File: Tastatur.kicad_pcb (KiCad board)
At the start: 2 copper layers, 74.8 x 41.4 mm, 86 parts, among them Q1 SI2301CDS-T1-GE3, Q2 2N7002HW, U1 CH592F, U3 AZ1117-3.3, U4 MT3608, U5 74LVC1G08, U6 LM393, U7 USBLC6-2SC6

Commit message: update power mgmt
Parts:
- removed D33, D4: LED, LED_SMD:LED_0603_1608Metric_Pad1.05x0.95mm_HandSolder
- removed D38, D39: CUS10S30,H3F, Diode_SMD:D_SOD-323
- removed R14, R15, R16, R17, R18, R19, R20, R21, R22, R23, R24, R25, R26, R27: 1 kohm, Resistor_SMD:R_0603_1608Metric_Pad0.98x0.95mm_HandSolder
- removed U2: ~, steew:ADNS-5090
- added C10: 100N, Capacitor_SMD:C_0603_1608Metric_Pad1.08x0.95mm_HandSolder, F.Cu at (168.6, 56.8)
- added C11: 100N, Capacitor_SMD:C_0603_1608Metric_Pad1.08x0.95mm_HandSolder, F.Cu at (168.6, 59.3)
- added C12: 100N, Capacitor_SMD:C_0603_1608Metric_Pad1.08x0.95mm_HandSolder, F.Cu at (168.6, 61.8)
- added C13: 100N, Capacitor_SMD:C_0603_1608Metric_Pad1.08x0.95mm_HandSolder, F.Cu at (168.6, 64.3)
- added C14: 100N, Capacitor_SMD:C_0603_1608Metric_Pad1.08x0.95mm_HandSolder, F.Cu at (172.9, 49.3)
- added C15: 100N, Capacitor_SMD:C_0603_1608Metric_Pad1.08x0.95mm_HandSolder, F.Cu at (172.9, 51.8)
- added C16: 100N, Capacitor_SMD:C_0603_1608Metric_Pad1.08x0.95mm_HandSolder, F.Cu at (172.9, 54.3)
- added C17: 100N, Capacitor_SMD:C_0603_1608Metric_Pad1.08x0.95mm_HandSolder, F.Cu at (172.9, 56.8)
- added C18: 100N, Capacitor_SMD:C_0603_1608Metric_Pad1.08x0.95mm_HandSolder, F.Cu at (172.9, 59.3)
- added C19: 100N, Capacitor_SMD:C_0603_1608Metric_Pad1.08x0.95mm_HandSolder, F.Cu at (172.9, 61.8)
- added C20: 100N, Capacitor_SMD:C_0603_1608Metric_Pad1.08x0.95mm_HandSolder, F.Cu at (172.9, 64.3)
- added C21: 100N, Capacitor_SMD:C_0603_1608Metric_Pad1.08x0.95mm_HandSolder, F.Cu at (177.3, 49.3)
- added C22: 100N, Capacitor_SMD:C_0603_1608Metric_Pad1.08x0.95mm_HandSolder, F.Cu at (147.4, 68.7)
- added C23: 100N, Capacitor_SMD:C_0603_1608Metric_Pad1.08x0.95mm_HandSolder, F.Cu at (177.3, 51.8)
- added C24: 100N, Capacitor_SMD:C_0603_1608Metric_Pad1.08x0.95mm_HandSolder, F.Cu at (177.3, 54.3)
- added C25: 100N, Capacitor_SMD:C_0603_1608Metric_Pad1.08x0.95mm_HandSolder, F.Cu at (177.3, 56.8)
- added C26: 100N, Capacitor_SMD:C_0603_1608Metric_Pad1.08x0.95mm_HandSolder, F.Cu at (177.3, 59.3)
- added C3: 22u, Capacitor_SMD:C_0603_1608Metric_Pad1.08x0.95mm_HandSolder, F.Cu at (79.3, 79.4)
- added C4: 22u, Capacitor_SMD:C_0603_1608Metric_Pad1.08x0.95mm_HandSolder, F.Cu at (79.3, 81.9)
- added C7: 100N, Capacitor_SMD:C_0603_1608Metric_Pad1.08x0.95mm_HandSolder, F.Cu at (168.6, 49.3)
- added C8: 100N, Capacitor_SMD:C_0603_1608Metric_Pad1.08x0.95mm_HandSolder, F.Cu at (168.6, 51.8)
- added C9: 100N, Capacitor_SMD:C_0603_1608Metric_Pad1.08x0.95mm_HandSolder, F.Cu at (168.6, 54.3)
- added D44: WS2812B, LED_SMD:LED_WS2812_PLCC6_5.0x5.0mm_P1.6mm, F.Cu at (162.3, 51.3)
- added D45: WS2812B, LED_SMD:LED_WS2812_PLCC6_5.0x5.0mm_P1.6mm, F.Cu at (162.3, 58.0)
- added D46: WS2812B, LED_SMD:LED_WS2812_PLCC6_5.0x5.0mm_P1.6mm, F.Cu at (162.3, 64.6)
- added D47: WS2812B, LED_SMD:LED_WS2812_PLCC6_5.0x5.0mm_P1.6mm, F.Cu at (162.3, 71.2)
- added J2: XT60PW-M, Connector_AMASS:AMASS_XT60PW-M_1x02_P7.20mm_Horizontal, F.Cu at (126.4, 65.4)
- added J3: XT60PW-F, Connector_AMASS:AMASS_XT60PW-F_1x02_P7.20mm_Horizontal, F.Cu at (151.8, 64.9)
- added L2: 4u7, Inductor_SMD:L_0603_1608Metric_Pad1.05x0.95mm_HandSolder, F.Cu at (79.3, 84.4)
- added Q3: SI2301CDS-T1-GE3, Package_TO_SOT_SMD:SOT-23_Handsoldering, F.Cu at (142.0, 70.0)
- added Q4: SI2301CDS-T1-GE3, Package_TO_SOT_SMD:SOT-23_Handsoldering, F.Cu at (142.0, 74.8)
- added Q5: SI2301CDS-T1-GE3, Package_TO_SOT_SMD:SOT-23_Handsoldering, F.Cu at (142.0, 79.5)
- added R9: 0R, Resistor_SMD:R_0603_1608Metric_Pad0.98x0.95mm_HandSolder, F.Cu at (114.7, 67.2)
- C1: value 100n -> 100N
- C5: value 10 µF -> 10u
- C6: value 22 µF -> 470u; footprint Capacitor_SMD:C_0603_1608Metric_Pad1.08x0.95mm_HandSolder -> Capacitor_SMD:CP_Elec_6.3x7.7
- D10, D14, D15, D16, D17, D22, D23, D24, D25, D3, D30, D31, D32, D8, D9: value LED -> WS2812B; footprint LED_SMD:LED_0603_1608Metric_Pad1.05x0.95mm_HandSolder -> LED_SMD:LED_WS2812_PLCC6_5.0x5.0mm_P1.6mm
- D2: value LED -> CD4148W; footprint LED_SMD:LED_0603_1608Metric_Pad1.05x0.95mm_HandSolder -> Diode_SMD:D_0805_2012Metric_Pad1.15x1.40mm_HandSolder
- R1, R2: value 5.1 kohm -> 5k1
- R10, R11, R12, R13: value 1 kohm -> 500R
- U3: value AZ1117-3.3 -> AP2112K-3.3; footprint Package_TO_SOT_SMD:TO-252-2 -> Package_TO_SOT_SMD:SOT-23-5_HandSoldering
- U5: value 74LVC1G08 -> CD4052B; footprint Package_TO_SOT_SMD:SOT-353_SC-70-5 -> Package_SO:TSSOP-16_4.4x5mm_P0.65mm
- moved C6 42.3 mm to (54.9, 83.0)
- moved U4 22.0 mm to (112.5, 84.5)
- moved Q2 22.0 mm to (112.9, 77.0)
- moved R4 22.0 mm to (101.3, 73.0)
- moved R6 22.0 mm to (101.3, 78.0)
- moved R7 22.0 mm to (101.3, 80.6)
- moved U3 22.0 mm to (110.4, 70.9)
- moved U5 22.0 mm to (117.2, 84.2)
- moved C1 22.0 mm to (101.3, 68.0)
- moved D40 22.0 mm to (112.7, 80.5)
- moved D41 22.0 mm to (101.2, 85.6)
- moved Q1 22.0 mm to (106.8, 77.4)
- moved R3 22.0 mm to (101.3, 70.5)
- moved R5 22.0 mm to (101.3, 75.5)
- moved R8 22.0 mm to (101.3, 83.1)
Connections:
- C6 pad 1: +3V3USB -> +3.3V
- D10 pad 1: GND -> +5V
- D10 pad 2: Net-(D10-A) -> Net-(D10-DOUT)
- D11 pad 1: /ROW0 -> /COL0
- D14 pad 1: GND -> +5V
- D14 pad 2: Net-(D14-A) -> unconnected-(D14-DOUT-Pad2)
- D15 pad 1: GND -> +5V
- D15 pad 2: Net-(D15-A) -> Net-(D15-DOUT)
- D16 pad 1: GND -> +5V
- D16 pad 2: Net-(D16-A) -> Net-(D16-DOUT)
- D17 pad 1: GND -> +5V
- D17 pad 2: Net-(D17-A) -> Net-(D17-DOUT)
- D18 pad 1: /ROW0 -> /COL0
- D2 pad 1: GND -> /ROW3
- D22 pad 1: GND -> +5V
- D22 pad 2: Net-(D22-A) -> Net-(D22-DOUT)
- D23 pad 1: GND -> +5V
- D23 pad 2: Net-(D23-A) -> unconnected-(D23-DOUT-Pad2)
- D24 pad 1: GND -> +5V
- D24 pad 2: Net-(D24-A) -> Net-(D24-DOUT)
- D25 pad 1: GND -> +5V
- D25 pad 2: Net-(D25-A) -> Net-(D25-DOUT)
- D26 pad 1: /ROW0 -> /COL0
- D3 pad 1: GND -> +5V
- D3 pad 2: Net-(D3-A) -> Net-(D3-DOUT)
- D30 pad 1: GND -> +5V
- D30 pad 2: Net-(D30-A) -> Net-(D30-DOUT)
- D31 pad 1: GND -> +5V
- D31 pad 2: Net-(D31-A) -> Net-(D31-DOUT)
- D32 pad 1: GND -> +5V
- D32 pad 2: Net-(D32-A) -> unconnected-(D32-DOUT-Pad2)
- D34 pad 1: /ROW0 -> /COL0
- D5 pad 1: /ROW0 -> /COL0
- D8 pad 1: GND -> +5V
- D8 pad 2: Net-(D8-A) -> Net-(D8-DOUT)
- D9 pad 1: GND -> +5V
- D9 pad 2: Net-(D9-A) -> Net-(D10-DIN)
- F1 pad 2: Net-(U3-VI) -> Net-(U3-VIN)
- R10 pad 1: /Matrix/LED_DRIVE -> /Matrix/LEDDATA0
- R10 pad 2: Net-(D2-A) -> Net-(D3-DIN)
- R11 pad 1: /Matrix/LED_DRIVE -> /Matrix/LEDDATA1
- R11 pad 2: Net-(D3-A) -> Net-(D15-DIN)
- R12 pad 1: /Matrix/LED_DRIVE -> /Matrix/LEDDATA2
- R12 pad 2: Net-(D4-A) -> Net-(D24-DIN)
- R13 pad 1: /Matrix/LED_DRIVE -> /Matrix/LEDDATA3
- R13 pad 2: Net-(D8-A) -> Net-(D44-DIN)
- TP4 pad 1: Net-(U3-VI) -> Net-(U3-VIN)
- U1 pad 1: /COL1 -> /COL0
- U1 pad 12: unconnected-(U1-UD+-Pad12) -> /D+
- U1 pad 13: unconnected-(U1-UD--Pad13) -> /D-
- U1 pad 14: /ROW0 -> /COL0
- U1 pad 15: unconnected-(U1-PB4-Pad15) -> /LEDDATA
- U1 pad 2: /COL2 -> /COL0
- U1 pad 21: unconnected-(U1-ANT-Pad21) -> Net-(AE1-A)
- U1 pad 23: unconnected-(U1-PA4-Pad23) -> /LEDSEL0
- U1 pad 28: /COL4 -> /COL0
- U1 pad 6: unconnected-(U1-PA8-Pad6) -> /LEDSEL1
- U1 pad 7: /COL3 -> /COL0
- U3 pad 1: GND -> Net-(U3-VIN)
- U3 pad 2: +3V3USB -> GND
- U3 pad 3: Net-(U3-VI) -> Net-(U3-EN)
- U4 pad 1: unconnected-(U4-SW-Pad1) -> Net-(U4-SW)
- U4 pad 2: unconnected-(U4-GND-Pad2) -> GND
- U4 pad 4: unconnected-(U4-EN-Pad4) -> /LEDTOGGLE
- U4 pad 5: unconnected-(U4-IN-Pad5) -> +3.3V
- U5 pad 1: +3.3VBAT -> GND
- U5 pad 2: unconnected-(U5-Pad2) -> GND
- U5 pad 3: unconnected-(U5-GND-Pad3) -> GND
- U5 pad 4: unconnected-(U5-Pad4) -> GND
- U5 pad 5: unconnected-(U5-VCC-Pad5) -> GND
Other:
- board size 74.8 x 41.4 mm -> 142.2 x 41.4 mm

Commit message: finish preliminary schematic
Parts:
- removed J3: XT60PW-F, Connector_AMASS:AMASS_XT60PW-F_1x02_P7.20mm_Horizontal
- added C2: 10u, Capacitor_SMD:C_0603_1608Metric_Pad1.08x0.95mm_HandSolder, F.Cu at (64.3, 93.3)
- added C27: 22u, Capacitor_SMD:C_0603_1608Metric_Pad1.08x0.95mm_HandSolder, F.Cu at (64.3, 95.8)
- added D33: GREEN, LED_SMD:LED_0603_1608Metric, F.Cu at (74.9, 95.9)
- added D38: LMBR130T1G, Diode_SMD:D_SOD-123, F.Cu at (69.3, 107.8)
- added D4: RED, LED_SMD:LED_0603_1608Metric, F.Cu at (74.9, 93.3)
- added Q6: SI2301CDS-T1-GE3, Package_TO_SOT_SMD:SOT-23_Handsoldering, F.Cu at (69.7, 94.5)
- added Q7: SI2301CDS-T1-GE3, Package_TO_SOT_SMD:SOT-23_Handsoldering, F.Cu at (69.7, 99.3)
- added R14: 330R, Resistor_SMD:R_0603_1608Metric_Pad0.98x0.95mm_HandSolder, F.Cu at (64.3, 98.3)
- added R15: 330R, Resistor_SMD:R_0603_1608Metric_Pad0.98x0.95mm_HandSolder, F.Cu at (64.3, 100.8)
- added R16: 2k2, Resistor_SMD:R_0603_1608Metric_Pad0.98x0.95mm_HandSolder, F.Cu at (64.3, 103.3)
- added R17: 110k, Resistor_SMD:R_0603_1608Metric_Pad0.98x0.95mm_HandSolder, F.Cu at (64.3, 105.8)
- added R18: 15k, Resistor_SMD:R_0603_1608Metric_Pad0.98x0.95mm_HandSolder, F.Cu at (64.3, 108.3)
- added U2: TP4056-42-ESOP8, Package_TO_SOT_SMD:TSOT-23-6_HandSoldering, F.Cu at (69.9, 103.9)
- C1, C10, C11, C12, C13, C14, C15, C16, C17, C18, C19, C20, C21, C22, C23, C24, C25, C26, C7, C8, C9: value 100N -> 100n
- D10, D14, D15, D16, D17, D22, D23, D24, D25, D3, D30, D31, D32, D44, D45, D46, D47, D8, D9: footprint LED_SMD:LED_WS2812_PLCC6_5.0x5.0mm_P1.6mm -> LED_SMD:LED_WS2812B_PLCC4_5.0x5.0mm_P3.2mm
- D11, D12, D13, D18, D19, D2, D20, D21, D26, D27, D28, D29, D34, D35, D36, D37, D5, D6, D7: value CD4148W -> RB521CS-30; footprint Diode_SMD:D_0805_2012Metric_Pad1.15x1.40mm_HandSolder -> Diode_SMD:D_SOD-923
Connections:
- net +3.3V renamed +3V3
- net +3.3VBAT renamed +3V3BAT
- net Net-(U3-VIN) renamed +5VUSB
- U4 pad 3: unconnected-(U4-FB-Pad3) -> Net-(U4-FB)
- U5 pad 6: /LEDSWITCH -> /LEDTOGGLE

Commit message: finish initial placement
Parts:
- removed C1, C10, C11, C12, C13, C14, C15, C16, C17, C18, C19, C20, C21, C22, C23, C24, C25, C26, C7, C8, C9: 100n, Capacitor_SMD:C_0603_1608Metric_Pad1.08x0.95mm_HandSolder
- removed C2, C5: 10u, Capacitor_SMD:C_0603_1608Metric_Pad1.08x0.95mm_HandSolder
- removed C27, C3, C4: 22u, Capacitor_SMD:C_0603_1608Metric_Pad1.08x0.95mm_HandSolder
- removed C6: 470u, Capacitor_SMD:CP_Elec_6.3x7.7
- removed D1: CPDUR5V0HE-HF, Diode_SMD:D_0603_1608Metric_Pad1.05x0.95mm_HandSolder
- removed D10, D14, D15, D16, D17, D22, D23, D24, D25, D3, D30, D31, D32, D44, D45, D46, D47, D8, D9: WS2812B, LED_SMD:LED_WS2812B_PLCC4_5.0x5.0mm_P3.2mm
- removed D11, D12, D13, D18, D19, D2, D20, D21, D26, D27, D28, D29, D34, D35, D36, D37, D5, D6, D7: RB521CS-30, Diode_SMD:D_SOD-923
- removed D33: GREEN, LED_SMD:LED_0603_1608Metric
- removed D38: LMBR130T1G, Diode_SMD:D_SOD-123
- removed D4, D41: RED, LED_SMD:LED_0603_1608Metric
- removed D40: DDZ9678-7, Diode_SMD:D_SOD-123F
- removed F1: 1812L050/30PR, Fuse:Fuse_1812_4532Metric_Pad1.30x3.40mm_HandSolder
- removed J2: XT60PW-M, Connector_AMASS:AMASS_XT60PW-M_1x02_P7.20mm_Horizontal
- removed L1: 120 Ohm @ 100 MHz, Inductor_SMD:L_0603_1608Metric_Pad1.05x0.95mm_HandSolder
- removed L2: 4u7, Inductor_SMD:L_0603_1608Metric_Pad1.05x0.95mm_HandSolder
- removed Q1, Q3, Q4, Q5, Q6, Q7: SI2301CDS-T1-GE3, Package_TO_SOT_SMD:SOT-23_Handsoldering
- removed Q2: 2N7002HW, Package_TO_SOT_SMD:SOT-323_SC-70_Handsoldering
- removed R1, R2: 5k1, Resistor_SMD:R_0603_1608Metric_Pad0.98x0.95mm_HandSolder
- removed R10, R11, R12, R13: 500R, Resistor_SMD:R_0603_1608Metric_Pad0.98x0.95mm_HandSolder
- removed R14, R15, R8: 330R, Resistor_SMD:R_0603_1608Metric_Pad0.98x0.95mm_HandSolder
- removed R16: 2k2, Resistor_SMD:R_0603_1608Metric_Pad0.98x0.95mm_HandSolder
- removed R17: 110k, Resistor_SMD:R_0603_1608Metric_Pad0.98x0.95mm_HandSolder
- removed R18: 15k, Resistor_SMD:R_0603_1608Metric_Pad0.98x0.95mm_HandSolder
- removed R3, R4: 50k, Resistor_SMD:R_0603_1608Metric_Pad0.98x0.95mm_HandSolder
- removed R5: 56k, Resistor_SMD:R_0603_1608Metric_Pad0.98x0.95mm_HandSolder
- removed R6: 160k, Resistor_SMD:R_0603_1608Metric_Pad0.98x0.95mm_HandSolder
- removed R7: 51k, Resistor_SMD:R_0603_1608Metric_Pad0.98x0.95mm_HandSolder
- removed R9: 0R, Resistor_SMD:R_0603_1608Metric_Pad0.98x0.95mm_HandSolder
- removed TP1, TP2, TP3, TP4: TestPoint, TestPoint:TestPoint_Pad_D1.0mm
- removed U1: CH592F, steew:CH592F
- removed U2: TP4056-42-ESOP8, Package_TO_SOT_SMD:TSOT-23-6_HandSoldering
- removed U3: AP2112K-3.3, Package_TO_SOT_SMD:SOT-23-5_HandSoldering
- removed U4: MT3608, Package_TO_SOT_SMD:SOT-23-6
- removed U5: CD4052B, Package_SO:TSSOP-16_4.4x5mm_P0.65mm
- removed U6: LM393, Package_SO:SOIC-8_3.9x4.9mm_P1.27mm
- removed U7: USBLC6-2SC6, Package_TO_SOT_SMD:SOT-23-6
- removed USB1: TYPE-C 16PIN 2MD(073), easyeda2kicad:USB-C-SMD_TYPE-C-6PIN-2MD-073
- added AE101: Antenna_Shield, Inductor_SMD:L_1206_3216Metric, F.Cu at (185.6, 99.3)
- added BT101: Battery_Cell, Battery:BatteryHolder_Keystone_1058_1x2032, B.Cu at (180.4, 117.1)
- added C101: 470n, Capacitor_SMD:C_0603_1608Metric_Pad1.08x0.95mm_HandSolder, F.Cu at (183.9, 105.7)
- added C102: 4u7, Capacitor_SMD:C_0603_1608Metric_Pad1.08x0.95mm_HandSolder, F.Cu at (174.4, 102.3)
- added C103: 100n, Capacitor_SMD:C_0603_1608Metric_Pad1.08x0.95mm_HandSolder, F.Cu at (184.0, 102.3)
- added C104: 2u2, Capacitor_SMD:C_0603_1608Metric_Pad1.08x0.95mm_HandSolder, F.Cu at (174.4, 103.9)
- added C105: 10p, Capacitor_SMD:C_0603_1608Metric_Pad1.08x0.95mm_HandSolder, F.Cu at (187.0, 102.3)
- added C106: 10p, Capacitor_SMD:C_0603_1608Metric_Pad1.08x0.95mm_HandSolder, F.Cu at (185.5, 102.3)
- added C107: 22u, Capacitor_SMD:C_0603_1608Metric_Pad1.08x0.95mm_HandSolder, F.Cu at (180.9, 133.0)
- added C108: 22u, Capacitor_SMD:C_0603_1608Metric_Pad1.08x0.95mm_HandSolder, F.Cu at (174.4, 127.5)
- added C109: 10u, Capacitor_SMD:C_0603_1608Metric_Pad1.08x0.95mm_HandSolder, F.Cu at (194.6, 129.0)
- added C110: 22u, Capacitor_SMD:C_0603_1608Metric_Pad1.08x0.95mm_HandSolder, F.Cu at (182.4, 133.0)
- added C111: 10u, Capacitor_SMD:C_0603_1608Metric_Pad1.08x0.95mm_HandSolder, F.Cu at (180.6, 109.4)
- added C112: 470u, Capacitor_SMD:CP_Elec_6.3x7.7, F.Cu at (190.8, 122.0)
- added C113: 100n, Capacitor_SMD:C_0603_1608Metric_Pad1.08x0.95mm_HandSolder, F.Cu at (174.4, 99.3)
- added C114: 100n, Capacitor_SMD:C_0603_1608Metric_Pad1.08x0.95mm_HandSolder, F.Cu at (180.1, 120.4)
- added C201: 100n, Capacitor_SMD:C_0603_1608Metric_Pad1.08x0.95mm_HandSolder, F.Cu at (79.2, 78.2)
- added C202: 100n, Capacitor_SMD:C_0603_1608Metric_Pad1.08x0.95mm_HandSolder, F.Cu at (99.2, 75.7)
- added C203: 100n, Capacitor_SMD:C_0603_1608Metric_Pad1.08x0.95mm_HandSolder, F.Cu at (119.2, 73.2)
- added C204: 100n, Capacitor_SMD:C_0603_1608Metric_Pad1.08x0.95mm_HandSolder, F.Cu at (139.2, 75.7)
- added C205: 100n, Capacitor_SMD:C_0603_1608Metric_Pad1.08x0.95mm_HandSolder, F.Cu at (159.2, 78.2)
- added C206: 100n, Capacitor_SMD:C_0603_1608Metric_Pad1.08x0.95mm_HandSolder, F.Cu at (79.2, 98.2)
- added C207: 100n, Capacitor_SMD:C_0603_1608Metric_Pad1.08x0.95mm_HandSolder, F.Cu at (99.2, 95.7)
- added C208: 100n, Capacitor_SMD:C_0603_1608Metric_Pad1.08x0.95mm_HandSolder, F.Cu at (119.2, 93.2)
- added C209: 100n, Capacitor_SMD:C_0603_1608Metric_Pad1.08x0.95mm_HandSolder, F.Cu at (139.2, 95.7)
- added C210: 100n, Capacitor_SMD:C_0603_1608Metric_Pad1.08x0.95mm_HandSolder, F.Cu at (159.2, 98.2)
- added C211: 100n, Capacitor_SMD:C_0603_1608Metric_Pad1.08x0.95mm_HandSolder, F.Cu at (79.2, 118.2)
- added C212: 100n, Capacitor_SMD:C_0603_1608Metric_Pad1.08x0.95mm_HandSolder, F.Cu at (99.2, 115.7)
- added C213: 100n, Capacitor_SMD:C_0603_1608Metric_Pad1.08x0.95mm_HandSolder, F.Cu at (119.2, 113.2)
- added C214: 100n, Capacitor_SMD:C_0603_1608Metric_Pad1.08x0.95mm_HandSolder, F.Cu at (139.2, 115.7)
- added C215: 100n, Capacitor_SMD:C_0603_1608Metric_Pad1.08x0.95mm_HandSolder, F.Cu at (159.2, 118.2)
- added C216: 100n, Capacitor_SMD:C_0603_1608Metric_Pad1.08x0.95mm_HandSolder, F.Cu at (99.2, 135.7)
- added C217: 100n, Capacitor_SMD:C_0603_1608Metric_Pad1.08x0.95mm_HandSolder, F.Cu at (119.2, 133.2)
- added C218: 100n, Capacitor_SMD:C_0603_1608Metric_Pad1.08x0.95mm_HandSolder, F.Cu at (139.2, 135.7)
- added C219: 100n, Capacitor_SMD:C_0603_1608Metric_Pad1.08x0.95mm_HandSolder, F.Cu at (159.2, 138.2)
- added D101: CPDUR5V0HE-HF, Diode_SMD:D_0603_1608Metric_Pad1.05x0.95mm_HandSolder, F.Cu at (196.2, 129.0)
- added D102: LMBR130T1G, Diode_SMD:D_SOD-123, F.Cu at (178.5, 128.0)
- added D103: GREEN, LED_SMD:LED_0603_1608Metric, F.Cu at (186.7, 112.0)
- added D104: RED, LED_SMD:LED_0603_1608Metric, F.Cu at (183.6, 112.0)
- added D105: DDZ9678-7, Diode_SMD:D_SOD-123F, F.Cu at (179.9, 116.9)
- added D106: RED, LED_SMD:LED_0603_1608Metric, F.Cu at (180.5, 112.0)
- added D201: RB521CS-30, Diode_SMD:D_SOD-923, F.Cu at (83.1, 78.4)
- added D202: RB521CS-30, Diode_SMD:D_SOD-923, F.Cu at (103.1, 75.9)
- added D203: RB521CS-30, Diode_SMD:D_SOD-923, F.Cu at (123.1, 73.4)
- added D204: RB521CS-30, Diode_SMD:D_SOD-923, F.Cu at (143.1, 75.9)
- added D205: RB521CS-30, Diode_SMD:D_SOD-923, F.Cu at (163.1, 78.4)
- added D206: RB521CS-30, Diode_SMD:D_SOD-923, F.Cu at (83.1, 98.4)
- added D207: RB521CS-30, Diode_SMD:D_SOD-923, F.Cu at (103.1, 95.9)
- added D208: RB521CS-30, Diode_SMD:D_SOD-923, F.Cu at (123.1, 93.4)
- added D209: RB521CS-30, Diode_SMD:D_SOD-923, F.Cu at (143.1, 95.9)
- added D210: RB521CS-30, Diode_SMD:D_SOD-923, F.Cu at (163.1, 98.4)
- added D211: RB521CS-30, Diode_SMD:D_SOD-923, F.Cu at (83.1, 118.4)
- added D212: RB521CS-30, Diode_SMD:D_SOD-923, F.Cu at (103.1, 115.9)
- added D213: RB521CS-30, Diode_SMD:D_SOD-923, F.Cu at (123.1, 113.4)
- added D214: RB521CS-30, Diode_SMD:D_SOD-923, F.Cu at (143.1, 115.9)
- added D215: RB521CS-30, Diode_SMD:D_SOD-923, F.Cu at (163.1, 118.4)
- added D216: RB521CS-30, Diode_SMD:D_SOD-923, F.Cu at (103.1, 135.9)
- added D217: RB521CS-30, Diode_SMD:D_SOD-923, F.Cu at (123.1, 133.4)
- added D218: RB521CS-30, Diode_SMD:D_SOD-923, F.Cu at (143.1, 135.9)
- added D219: RB521CS-30, Diode_SMD:D_SOD-923, F.Cu at (163.1, 138.4)
- added D251: SK6805-EC15, LED_SMD:LED_SK6812_EC15_1.5x1.5mm, F.Cu at (83.1, 75.1)
- added D252: SK6805-EC15, LED_SMD:LED_SK6812_EC15_1.5x1.5mm, F.Cu at (103.1, 72.6)
- added D253: SK6805-EC15, LED_SMD:LED_SK6812_EC15_1.5x1.5mm, F.Cu at (123.1, 70.1)
- added D254: SK6805-EC15, LED_SMD:LED_SK6812_EC15_1.5x1.5mm, F.Cu at (143.1, 72.6)
- added D255: SK6805-EC15, LED_SMD:LED_SK6812_EC15_1.5x1.5mm, F.Cu at (163.1, 75.1)
- added D256: SK6805-EC15, LED_SMD:LED_SK6812_EC15_1.5x1.5mm, F.Cu at (83.1, 95.1)
- added D257: SK6805-EC15, LED_SMD:LED_SK6812_EC15_1.5x1.5mm, F.Cu at (103.1, 92.6)
- added D258: SK6805-EC15, LED_SMD:LED_SK6812_EC15_1.5x1.5mm, F.Cu at (123.1, 90.1)
- added D259: SK6805-EC15, LED_SMD:LED_SK6812_EC15_1.5x1.5mm, F.Cu at (143.1, 92.6)
- added D260: SK6805-EC15, LED_SMD:LED_SK6812_EC15_1.5x1.5mm, F.Cu at (163.1, 95.1)
- added D261: SK6805-EC15, LED_SMD:LED_SK6812_EC15_1.5x1.5mm, F.Cu at (83.1, 115.1)
- added D262: SK6805-EC15, LED_SMD:LED_SK6812_EC15_1.5x1.5mm, F.Cu at (103.1, 112.6)
- added D263: SK6805-EC15, LED_SMD:LED_SK6812_EC15_1.5x1.5mm, F.Cu at (123.1, 110.1)
- added D264: SK6805-EC15, LED_SMD:LED_SK6812_EC15_1.5x1.5mm, F.Cu at (143.1, 112.6)
- added D265: SK6805-EC15, LED_SMD:LED_SK6812_EC15_1.5x1.5mm, F.Cu at (163.1, 115.1)
- added D266: SK6805-EC15, LED_SMD:LED_SK6812_EC15_1.5x1.5mm, F.Cu at (103.1, 132.6)
- added D267: SK6805-EC15, LED_SMD:LED_SK6812_EC15_1.5x1.5mm, F.Cu at (123.1, 130.1)
- added D268: SK6805-EC15, LED_SMD:LED_SK6812_EC15_1.5x1.5mm, F.Cu at (143.1, 132.6)
- added D269: SK6805-EC15, LED_SMD:LED_SK6812_EC15_1.5x1.5mm, F.Cu at (163.1, 135.1)
- added F101: 1812L050/30PR, Fuse:Fuse_1812_4532Metric_Pad1.30x3.40mm_HandSolder, F.Cu at (184.2, 128.7)
- added H201: MountingHole, MountingHole:MountingHole_2.2mm_M2_ISO7380, F.Cu at (90.2, 122.1)
- added H202: MountingHole, MountingHole:MountingHole_2.2mm_M2_ISO7380, F.Cu at (175.3, 90.1)
- added J102: Conn_01x04_Pin, Connector_JST:JST_PH_B4B-PH-K_1x04_P2.00mm_Vertical, F.Cu at (196.6, 123.1)
- added J103: XT60PW-M, Connector_AMASS:AMASS_XT60PW-M_1x02_P7.20mm_Horizontal, F.Cu at (191.2, 97.0)
- added L101: 10u, Inductor_SMD:L_0603_1608Metric_Pad1.05x0.95mm_HandSolder, F.Cu at (174.4, 100.8)
- added L102: 4u7, Inductor_SMD:L_0603_1608Metric_Pad1.05x0.95mm_HandSolder, F.Cu at (174.4, 129.1)
- added L103: 120 Ohm @ 100 MHz, Inductor_SMD:L_0603_1608Metric_Pad1.05x0.95mm_HandSolder, F.Cu at (193.1, 129.0)
- added Q101: SI2301CDS-T1-GE3, Package_TO_SOT_SMD:SOT-23_Handsoldering, F.Cu at (178.3, 123.9)
- added Q102: SI2301CDS-T1-GE3, Package_TO_SOT_SMD:SOT-23_Handsoldering, F.Cu at (174.8, 123.9)
- added Q103: SI2301CDS-T1-GE3, Package_TO_SOT_SMD:SOT-23_Handsoldering, F.Cu at (185.4, 123.9)
- added Q104: SI2301CDS-T1-GE3, Package_TO_SOT_SMD:SOT-23_Handsoldering, F.Cu at (186.5, 95.0)
- added Q105: SI2301CDS-T1-GE3, Package_TO_SOT_SMD:SOT-23_Handsoldering, F.Cu at (178.0, 106.9)
- added Q106: 2N7002HW, Package_TO_SOT_SMD:SOT-323_SC-70_Handsoldering, F.Cu at (174.3, 107.2)
- added Q107: SI2301CDS-T1-GE3, Package_TO_SOT_SMD:SOT-23_Handsoldering, F.Cu at (181.9, 123.9)
- added R101: 5k1, Resistor_SMD:R_0603_1608Metric_Pad0.98x0.95mm_HandSolder, F.Cu at (197.7, 129.0)
- added R102: 5k1, Resistor_SMD:R_0603_1608Metric_Pad0.98x0.95mm_HandSolder, F.Cu at (191.5, 129.0)
- added R103: 0R, Resistor_SMD:R_0603_1608Metric_Pad0.98x0.95mm_HandSolder, F.Cu at (185.5, 136.9)
- added R104: 110k, Resistor_SMD:R_0603_1608Metric_Pad0.98x0.95mm_HandSolder, F.Cu at (177.8, 132.9)
- added R105: 15k, Resistor_SMD:R_0603_1608Metric_Pad0.98x0.95mm_HandSolder, F.Cu at (179.4, 132.9)
- added R106: 330R, Resistor_SMD:R_0603_1608Metric_Pad0.98x0.95mm_HandSolder, F.Cu at (186.9, 113.8)
- added R107: 330R, Resistor_SMD:R_0603_1608Metric_Pad0.98x0.95mm_HandSolder, F.Cu at (183.6, 113.8)
- added R108: 50k, Resistor_SMD:R_0603_1608Metric_Pad0.98x0.95mm_HandSolder, F.Cu at (175.8, 111.6)
- added R109: 2k2, Resistor_SMD:R_0603_1608Metric_Pad0.98x0.95mm_HandSolder, F.Cu at (190.2, 109.7)
- added R110: 50k, Resistor_SMD:R_0603_1608Metric_Pad0.98x0.95mm_HandSolder, F.Cu at (174.2, 111.6)
- added R111: 33k, Resistor_SMD:R_0603_1608Metric_Pad0.98x0.95mm_HandSolder, F.Cu at (184.2, 119.3)
- added R112: 51k, Resistor_SMD:R_0603_1608Metric_Pad0.98x0.95mm_HandSolder, F.Cu at (182.7, 119.3)
- added R113: 56k, Resistor_SMD:R_0603_1608Metric_Pad0.98x0.95mm_HandSolder, F.Cu at (177.3, 111.6)
- added R114: 330R, Resistor_SMD:R_0603_1608Metric_Pad0.98x0.95mm_HandSolder, F.Cu at (180.3, 113.8)
- added R201: 500R, Resistor_SMD:R_0603_1608Metric_Pad0.98x0.95mm_HandSolder, F.Cu at (174.4, 94.7)
- added R202: 500R, Resistor_SMD:R_0603_1608Metric_Pad0.98x0.95mm_HandSolder, F.Cu at (174.4, 96.2)
- added R203: 500R, Resistor_SMD:R_0603_1608Metric_Pad0.98x0.95mm_HandSolder, F.Cu at (174.4, 97.8)
- added R204: 500R, Resistor_SMD:R_0603_1608Metric_Pad0.98x0.95mm_HandSolder, F.Cu at (174.4, 93.2)
- added R205: 50k, Resistor_SMD:R_0603_1608Metric_Pad0.98x0.95mm_HandSolder, F.Cu at (174.4, 134.1)
- added SW201: SW_Push, PCM_Switch_Keyboard_Cherry_MX:SW_Cherry_MX_PCB_1.00u, F.Cu at (83.1, 69.6)
- added SW202: SW_Push, PCM_Switch_Keyboard_Cherry_MX:SW_Cherry_MX_PCB_1.00u, F.Cu at (103.1, 67.1)
- added SW203: SW_Push, PCM_Switch_Keyboard_Cherry_MX:SW_Cherry_MX_PCB_1.00u, F.Cu at (123.1, 64.6)
- added SW204: SW_Push, PCM_Switch_Keyboard_Cherry_MX:SW_Cherry_MX_PCB_1.00u, F.Cu at (143.1, 67.1)
- added SW205: SW_Push, PCM_Switch_Keyboard_Cherry_MX:SW_Cherry_MX_PCB_1.00u, F.Cu at (163.1, 69.6)
- added SW206: SW_Push, PCM_Switch_Keyboard_Cherry_MX:SW_Cherry_MX_PCB_1.00u, F.Cu at (83.1, 89.6)
- added SW207: SW_Push, PCM_Switch_Keyboard_Cherry_MX:SW_Cherry_MX_PCB_1.00u, F.Cu at (103.1, 87.1)
- added SW208: SW_Push, PCM_Switch_Keyboard_Cherry_MX:SW_Cherry_MX_PCB_1.00u, F.Cu at (123.1, 84.6)
- added SW209: SW_Push, PCM_Switch_Keyboard_Cherry_MX:SW_Cherry_MX_PCB_1.00u, F.Cu at (143.1, 87.1)
- added SW210: SW_Push, PCM_Switch_Keyboard_Cherry_MX:SW_Cherry_MX_PCB_1.00u, F.Cu at (163.1, 89.6)
- added SW211: SW_Push, PCM_Switch_Keyboard_Cherry_MX:SW_Cherry_MX_PCB_1.00u, F.Cu at (83.1, 109.6)
- added SW212: SW_Push, PCM_Switch_Keyboard_Cherry_MX:SW_Cherry_MX_PCB_1.00u, F.Cu at (103.1, 107.1)
- added SW213: SW_Push, PCM_Switch_Keyboard_Cherry_MX:SW_Cherry_MX_PCB_1.00u, F.Cu at (123.1, 104.6)
- added SW214: SW_Push, PCM_Switch_Keyboard_Cherry_MX:SW_Cherry_MX_PCB_1.00u, F.Cu at (143.1, 107.1)
- added SW215: SW_Push, PCM_Switch_Keyboard_Cherry_MX:SW_Cherry_MX_PCB_1.00u, F.Cu at (163.1, 109.6)
- added SW216: SW_Push, PCM_Switch_Keyboard_Cherry_MX:SW_Cherry_MX_PCB_1.00u, F.Cu at (103.1, 127.1)
- added SW217: SW_Push, PCM_Switch_Keyboard_Cherry_MX:SW_Cherry_MX_PCB_1.00u, F.Cu at (123.1, 124.6)
- added SW218: SW_Push, PCM_Switch_Keyboard_Cherry_MX:SW_Cherry_MX_PCB_1.00u, F.Cu at (143.1, 127.1)
- added SW219: SW_Push, PCM_Switch_Keyboard_Cherry_MX:SW_Cherry_MX_PCB_1.00u, F.Cu at (163.1, 129.6)
- added SW221: MK-12C02-G020, Button_Switch_SMD:SW_SPDT_PCM12, F.Cu at (177.3, 137.5)
- added TP101: TestPoint, TestPoint:TestPoint_Pad_D1.0mm, F.Cu at (195.9, 110.2)
- added TP103: TestPoint, TestPoint:TestPoint_Pad_D1.0mm, F.Cu at (195.9, 112.7)
- added TP104: TestPoint, TestPoint:TestPoint_Pad_D1.0mm, F.Cu at (193.8, 111.5)
- added U101: USBLC6-2SC6, Package_TO_SOT_SMD:SOT-23-6, F.Cu at (189.0, 128.7)
- added U102: CH592F, steew:CH592F, F.Cu at (179.8, 101.5)
- added U103: AP2112K-3.3, Package_TO_SOT_SMD:SOT-23-5_HandSoldering, F.Cu at (185.6, 132.9)
- added U104: MT3608, Package_TO_SOT_SMD:SOT-23-6, F.Cu at (174.8, 131.6)
- added U105: TP4056-42-ESOP8, Package_TO_SOT_SMD:TSOT-23-6_HandSoldering, F.Cu at (185.3, 109.5)
- added U106: CD4052B, Package_SO:TSSOP-16_4.4x5mm_P0.65mm, F.Cu at (180.1, 95.2)
- added U107: LM393, Package_SO:SOIC-8_3.9x4.9mm_P1.27mm, F.Cu at (175.8, 117.3)
- added USB101: TYPE-C 16PIN 2MD(073), easyeda2kicad:USB-C-SMD_TYPE-C-6PIN-2MD-073, F.Cu at (193.1, 136.0)
- added Y101: 32MHz, Crystal:Crystal_SMD_2016-4Pin_2.0x1.6mm, F.Cu at (186.2, 105.2)
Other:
- board size 142.2 x 41.4 mm -> 125.5 x 85.1 mm

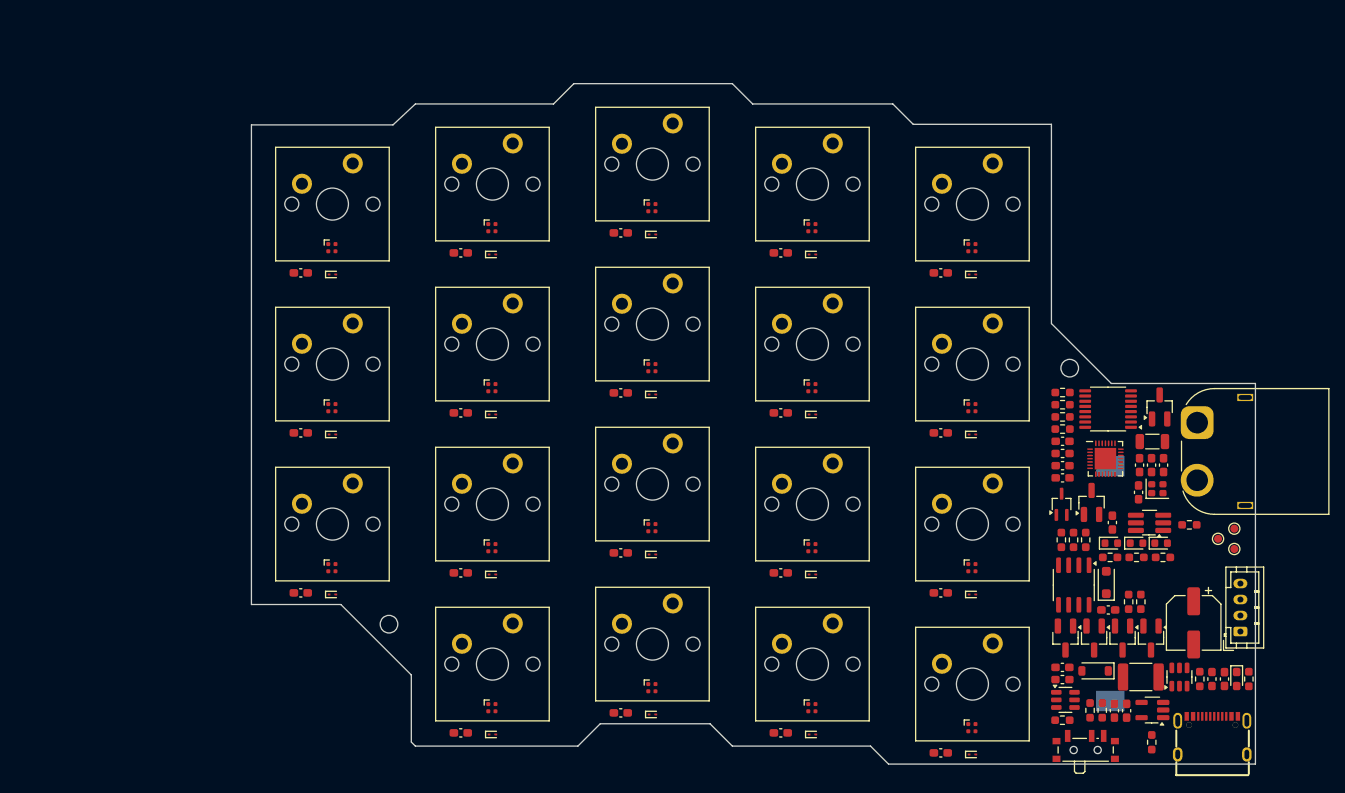
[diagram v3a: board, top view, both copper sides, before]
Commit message: start routing power
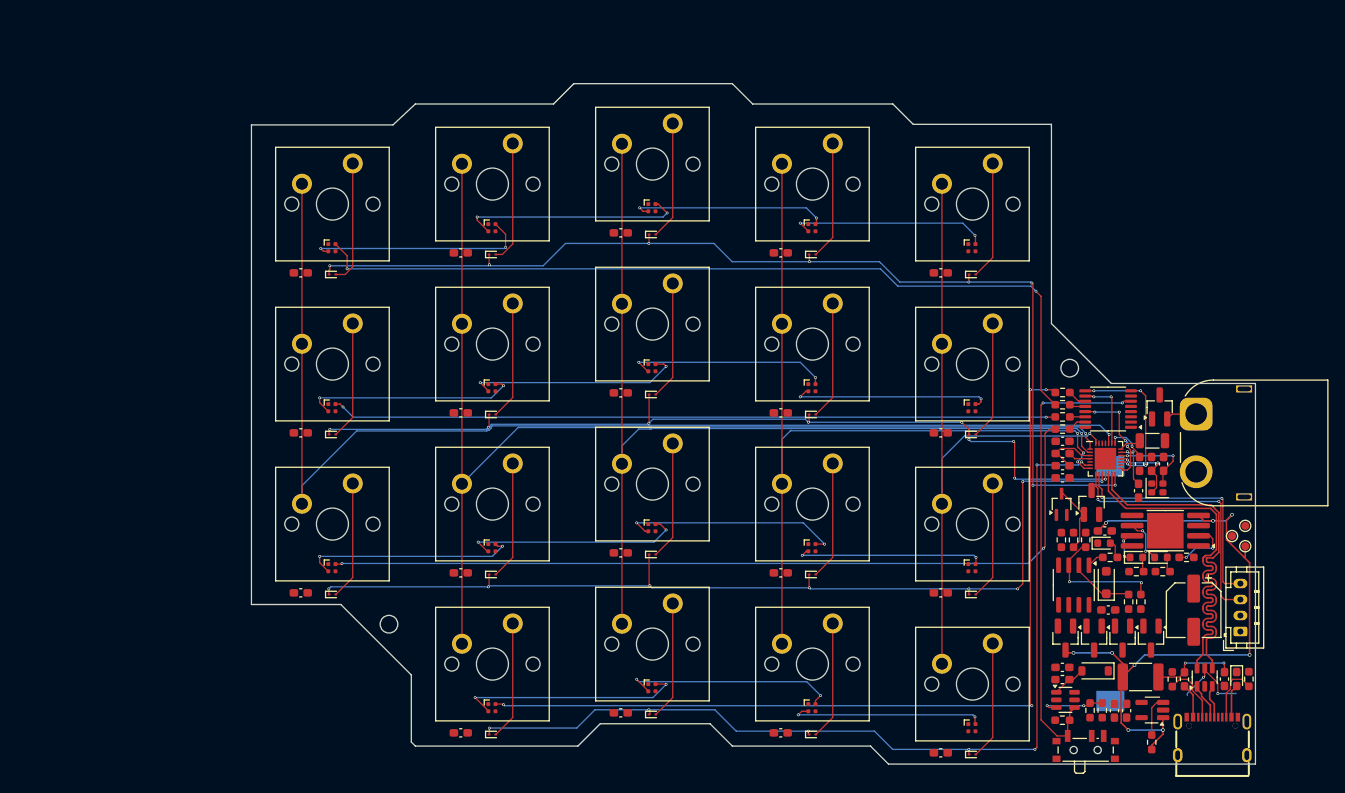
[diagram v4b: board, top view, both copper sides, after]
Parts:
- U105: footprint Package_TO_SOT_SMD:TSOT-23-6_HandSoldering -> Package_SO:SOP-8-1EP_4.57x4.57mm_P1.27mm_EP4.57x4.45mm
- moved R109 4.08 mm to (189.9, 113.8)
- moved L103 3.43 mm to (189.6, 129.0)
- moved R102 3.43 mm to (188.1, 129.0)
- moved U101 3.16 mm to (192.2, 128.8)
- moved U105 2.20 mm to (187.2, 110.5)
- moved TP104 1.78 mm to (195.6, 111.1)
- moved D103 1.78 mm to (186.7, 113.8)
- moved D104 1.78 mm to (183.6, 113.8)
- moved R106 1.78 mm to (186.9, 115.6)
- moved R107 1.78 mm to (183.6, 115.6)
- moved C112 1.59 mm to (190.8, 120.4)
- moved C111 1.41 mm to (179.7, 110.5), turned to 180 degrees
- moved TP103 1.41 mm to (197.2, 112.4)
- moved TP101 1.41 mm to (197.2, 109.9)
- moved J103 1.07 mm to (191.1, 95.9)
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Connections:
- net Net-(J102-Pin_3) renamed /TCK
- net Net-(J102-Pin_4) renamed /TIO
- U102 pad 17: /ROW3 -> /LEDSEL1
- U102 pad 6: /LEDSEL1 -> /ROW3
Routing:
- net /COL0: track 0.00 -> 148.0 mm, vias 0 -> 1
- net /COL1: track 0.00 -> 143.4 mm, vias 0 -> 1
- net /ROW0: track 0.00 -> 133.5 mm, vias 0 -> 8
- net /COL2: track 0.00 -> 123.8 mm, vias 0 -> 1
- net /ROW2: track 0.00 -> 119.7 mm, vias 0 -> 8
- net /ROW3: track 0.00 -> 116.4 mm, vias 0 -> 7
- net /ROW1: track 0.00 -> 111.5 mm, vias 0 -> 9
- net Net-(D266-DIN): track 0.00 -> 110.0 mm, vias 0 -> 4
- net /COL3: track 0.00 -> 109.3 mm, vias 0 -> 3
- net Net-(D251-DIN): track 0.00 -> 106.2 mm, vias 0 -> 2
- net Net-(D261-DIN): track 0.00 -> 105.3 mm, vias 0 -> 2
- net Net-(D256-DIN): track 0.00 -> 90.7 mm, vias 0 -> 2
- net /COL4: track 0.00 -> 87.0 mm, vias 0 -> 1
- net +5VUSB: track 0.00 -> 82.7 mm, vias 0 -> 9
- net /LEDTOGGLE: track 0.00 -> 59.6 mm, vias 0 -> 2
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
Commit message: halfway new routing
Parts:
- moved C103 4.30 mm to (186.4, 98.6), turned to 180 degrees
- moved C105 3.94 mm to (184.7, 105.3), turned to -90 degrees
- moved C106 3.94 mm to (183.2, 105.3), turned to -90 degrees
- moved C101 3.81 mm to (186.4, 102.6), turned to 180 degrees
- moved R103 1.55 mm to (186.4, 135.6), turned to 0 degrees
- moved TP104 1.53 mm to (197.1, 111.3)
- moved C102 1.52 mm to (174.4, 100.8)
- moved L101 1.52 mm to (174.4, 102.3)
- moved AE101 1.41 mm to (185.9, 100.6)
- moved TP103 1.15 mm to (197.1, 113.5)
- moved TP101 0.89 mm to (197.2, 109.0)
- moved Y101 0.67 mm to (186.9, 104.9)
- moved R110 0.51 mm to (173.7, 111.6)
- moved R108 0.25 mm to (175.5, 111.6)
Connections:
- SW221 pad 2: +3.3VBAT -> +3V3BAT
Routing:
- net +5V: track 0.00 -> 140.8 mm, vias 0 -> 2
- net +3V3: track 0.00 -> 114.1 mm, vias 0 -> 13
- net Net-(D266-DIN): track 110.0 -> 0.00 mm, vias 4 -> 0
- net /COL0: track 148.0 -> 40.2 mm, vias 1 -> 0
- net Net-(D251-DIN): track 106.2 -> 0.00 mm, vias 2 -> 0
- net Net-(D261-DIN): track 105.3 -> 0.00 mm, vias 2 -> 0
- net Net-(D256-DIN): track 90.7 -> 0.00 mm, vias 2 -> 0
- net /COL1: track 143.4 -> 60.3 mm, vias 1 -> 0
- net /COL2: track 123.8 -> 60.4 mm, vias 1 -> 0
- net /VBAT: track 0.00 -> 59.3 mm, vias 0 -> 6
- net +3V3BAT: track 0.00 -> 57.5 mm, vias 0 -> 6
- net +3V3USB: track 0.00 -> 55.8 mm, vias 0 -> 5
- net /COL3: track 109.3 -> 60.3 mm, vias 3 -> 0
- net /ROW0: track 133.5 -> 89.6 mm, vias 8 -> 5
- net /ROW3: track 116.4 -> 75.5 mm, vias 7 -> 4
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- added copper zone on B.Cu, net GND
- added copper zone on F.Cu, net GND

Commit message: final routing
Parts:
- moved Q105 0.22 mm to (177.8, 106.9)
- moved AE101 0.21 mm to (186.0, 100.4)
- moved J103 0.19 mm to (190.9, 95.9)
- moved C103 0.10 mm to (186.4, 98.5)
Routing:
- net +5V: track 140.8 -> 603.9 mm, vias 2 -> 34
- net Net-(D251-DIN): track 0.00 -> 112.4 mm, vias 0 -> 2
- net GND: track 0.00 -> 111.4 mm, vias 0 -> 34
- net Net-(D266-DIN): track 0.00 -> 111.0 mm, vias 0 -> 4
- net Net-(D261-DIN): track 0.00 -> 109.8 mm, vias 0 -> 4
- net /COL0: track 40.2 -> 146.1 mm, vias 0 -> 4
- net Net-(D256-DIN): track 0.00 -> 91.6 mm, vias 0 -> 2
- net /COL1: track 60.3 -> 140.3 mm, vias 0 -> 2
- net /COL2: track 60.4 -> 119.8 mm, vias 0 -> 1
- net /ROW3: track 75.5 -> 131.2 mm, vias 4 -> 7
- net /ROW0: track 89.6 -> 143.3 mm, vias 5 -> 8
- net /COL3: track 60.3 -> 100.3 mm, vias 0 -> 1
- net /ROW2: track 88.8 -> 118.7 mm, vias 5 -> 8
- net /ROW1: track 89.5 -> 119.2 mm, vias 5 -> 8
- net /LEDSEL1: track 0.00 -> 16.6 mm, vias 0 -> 2
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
